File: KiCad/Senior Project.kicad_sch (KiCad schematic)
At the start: 20 parts, among them J1 B2B-PH-K-S, J3 Screw_Terminal_01x06, J4 Conn_ARM_JTAG_SWD_10, J5 Conn_01x03, J6 Conn_01x02, J7 USB4105-GF-A, SW1 SW_Push, U1 ESP32-S3-WROOM-1

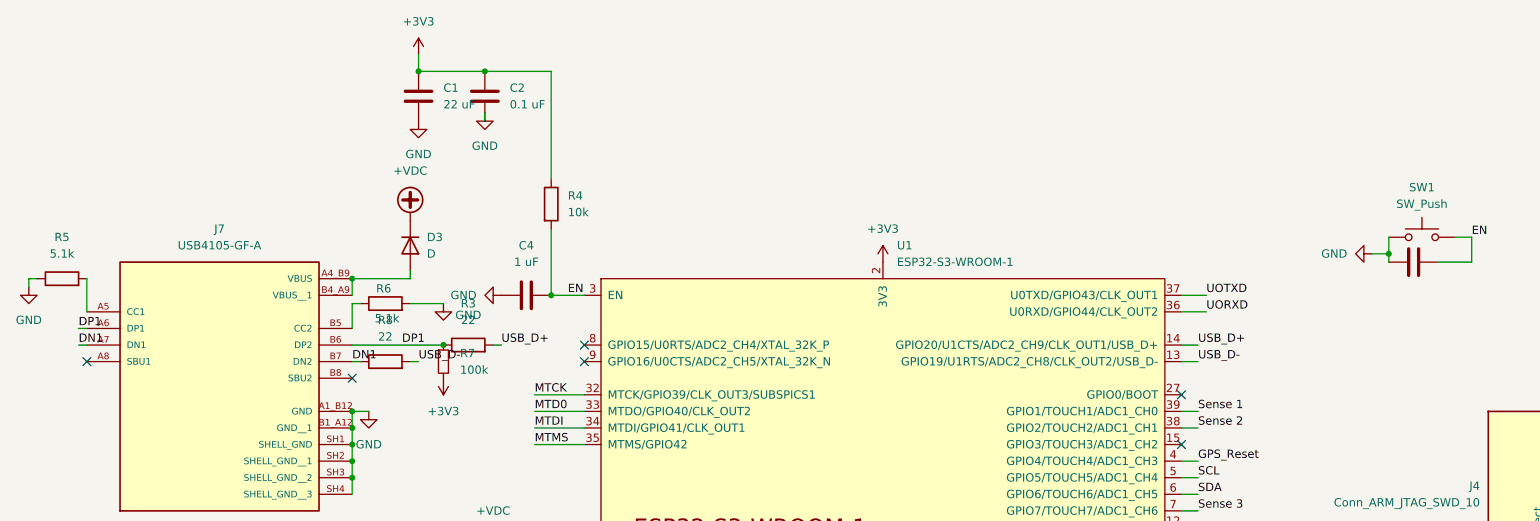
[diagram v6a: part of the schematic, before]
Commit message: Switch added, LCSC table, other changes.
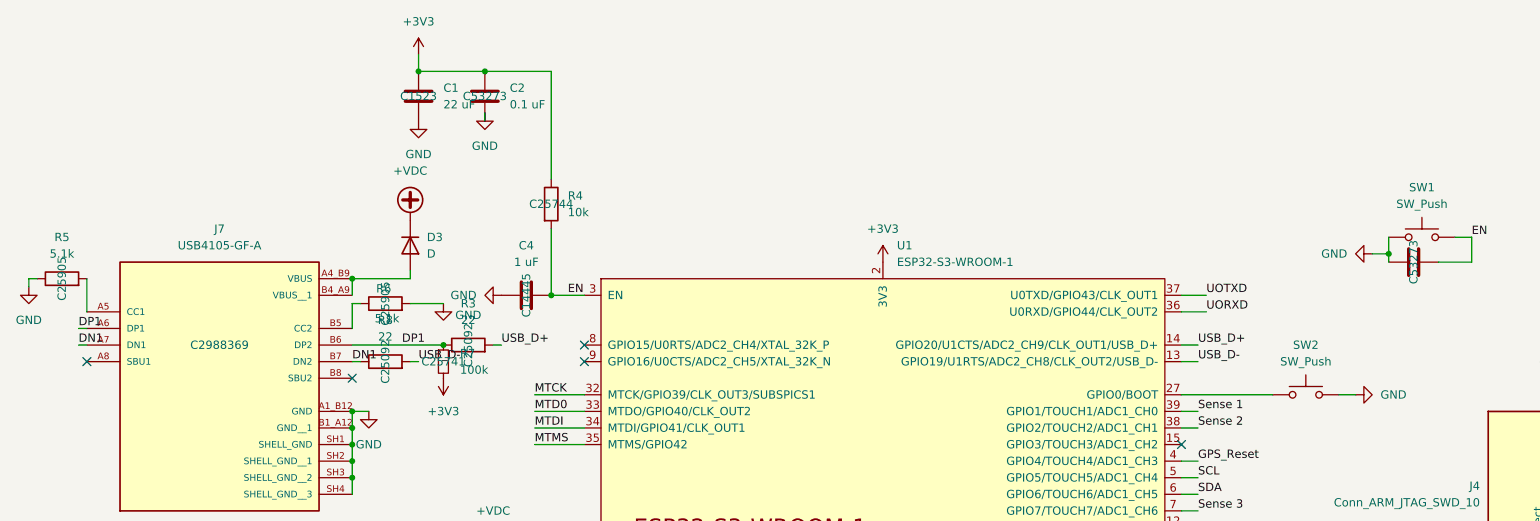
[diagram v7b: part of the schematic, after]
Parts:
- added SW2: SW_Push, Button_Switch_SMD:SW_SPST_PTS810, symbol Switch:SW_Push
- C1: LCSC (none) -> C1523
- C2, C3: LCSC (none) -> C53273
- C4: LCSC (none) -> C14445
- J7: LCSC (none) -> C2988369
- R3, R8: LCSC (none) -> C25092
- R4: LCSC (none) -> C25744
- R5, R6: LCSC (none) -> C25905
- R7: LCSC (none) -> C25741
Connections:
- net GND: now also SW2.2
- net at U1.27 (GPIO0/BOOT): now also SW2.1
- no-connect marks 17 -> 16

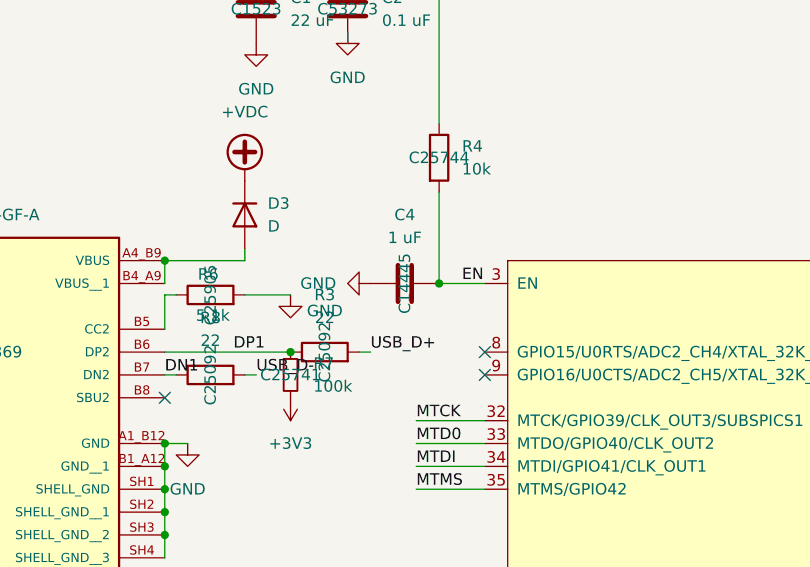
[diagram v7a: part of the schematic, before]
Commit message: Footprints added and small changes
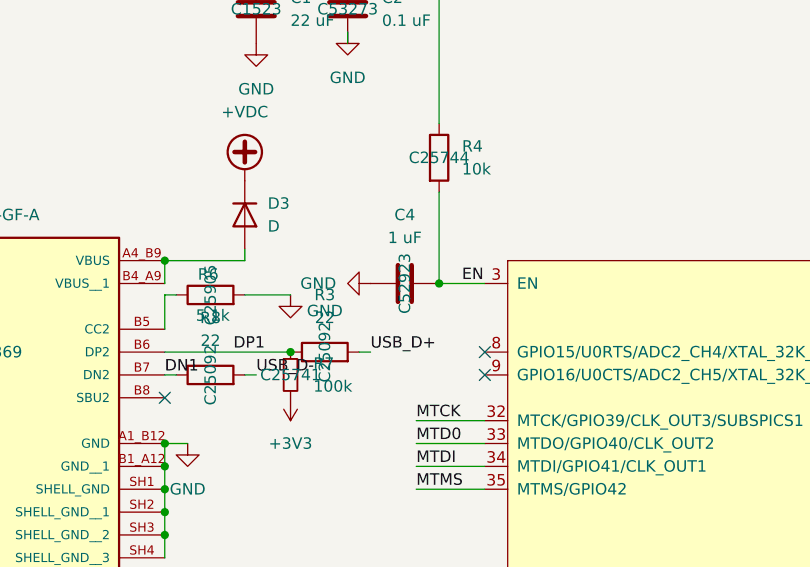
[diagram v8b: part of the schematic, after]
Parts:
- C4: LCSC C14445 -> C52923
- J1: footprint CONN2_B2B-PH-K-S_JST -> JST_Connector:CONN2_B2B-PH-K-S_JST
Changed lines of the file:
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@@
 			)
 		)
-		(property "Footprint" "CONN2_B2B-PH-K-S_JST"
+		(property "Footprint" "JST_Connector:CONN2_B2B-PH-K-S_JST"
 			(at 68.58 101.6 0)
 			(effects
@@
 			)
 		)
-		(property "LCSC" "C14445"
+		(property "LCSC" "C52923"
 			(at 93.98 55.88 0)
 			(effects
